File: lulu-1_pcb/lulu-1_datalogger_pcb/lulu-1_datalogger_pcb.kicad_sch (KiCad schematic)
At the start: 37 parts, among them J1 Conn_01x02_Pin, J2 SBH11-PBPC-D10-ST-BK, J3 MEM2067-02-180-00-A_REVB, SW1 SW_Nidec_CAS-120A1, U1 LP3982ILD-3.3, U2 STM32F401RETx, U3 BMP280, U4 MPU-6050, U5 W25Q16JVSS, Y1 25 Mhz, Y2 32 Khz

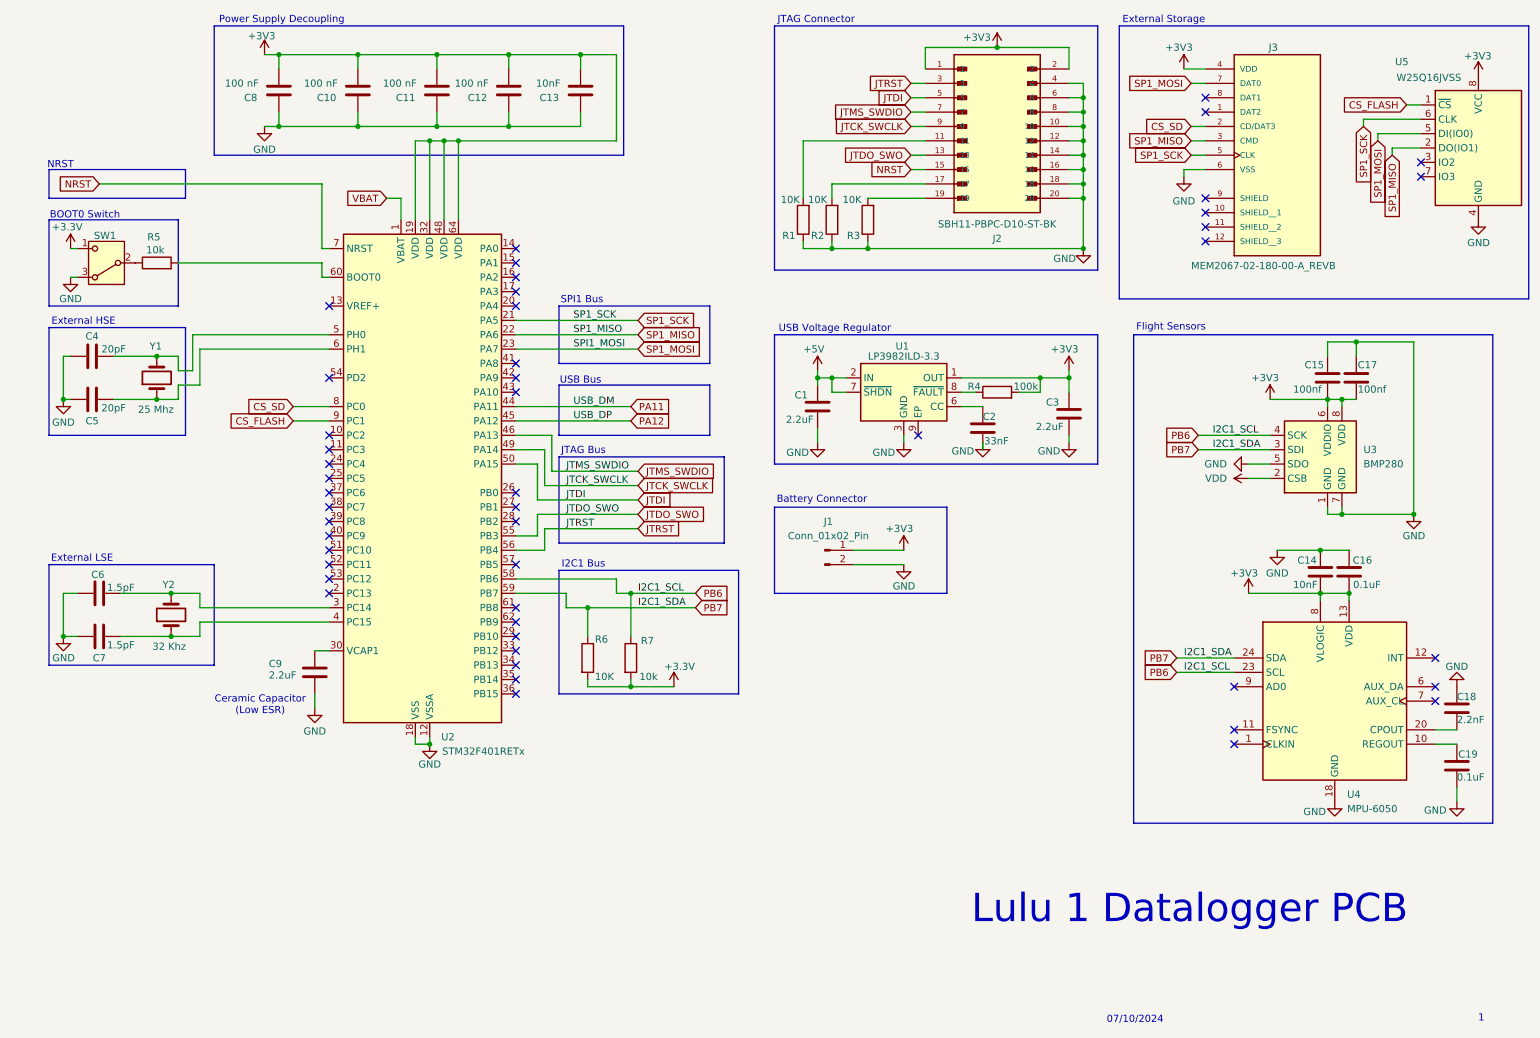
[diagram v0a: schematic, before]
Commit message: label for SPI chip select pins and remvoed VBAT and merged with +3V3/VDD pins
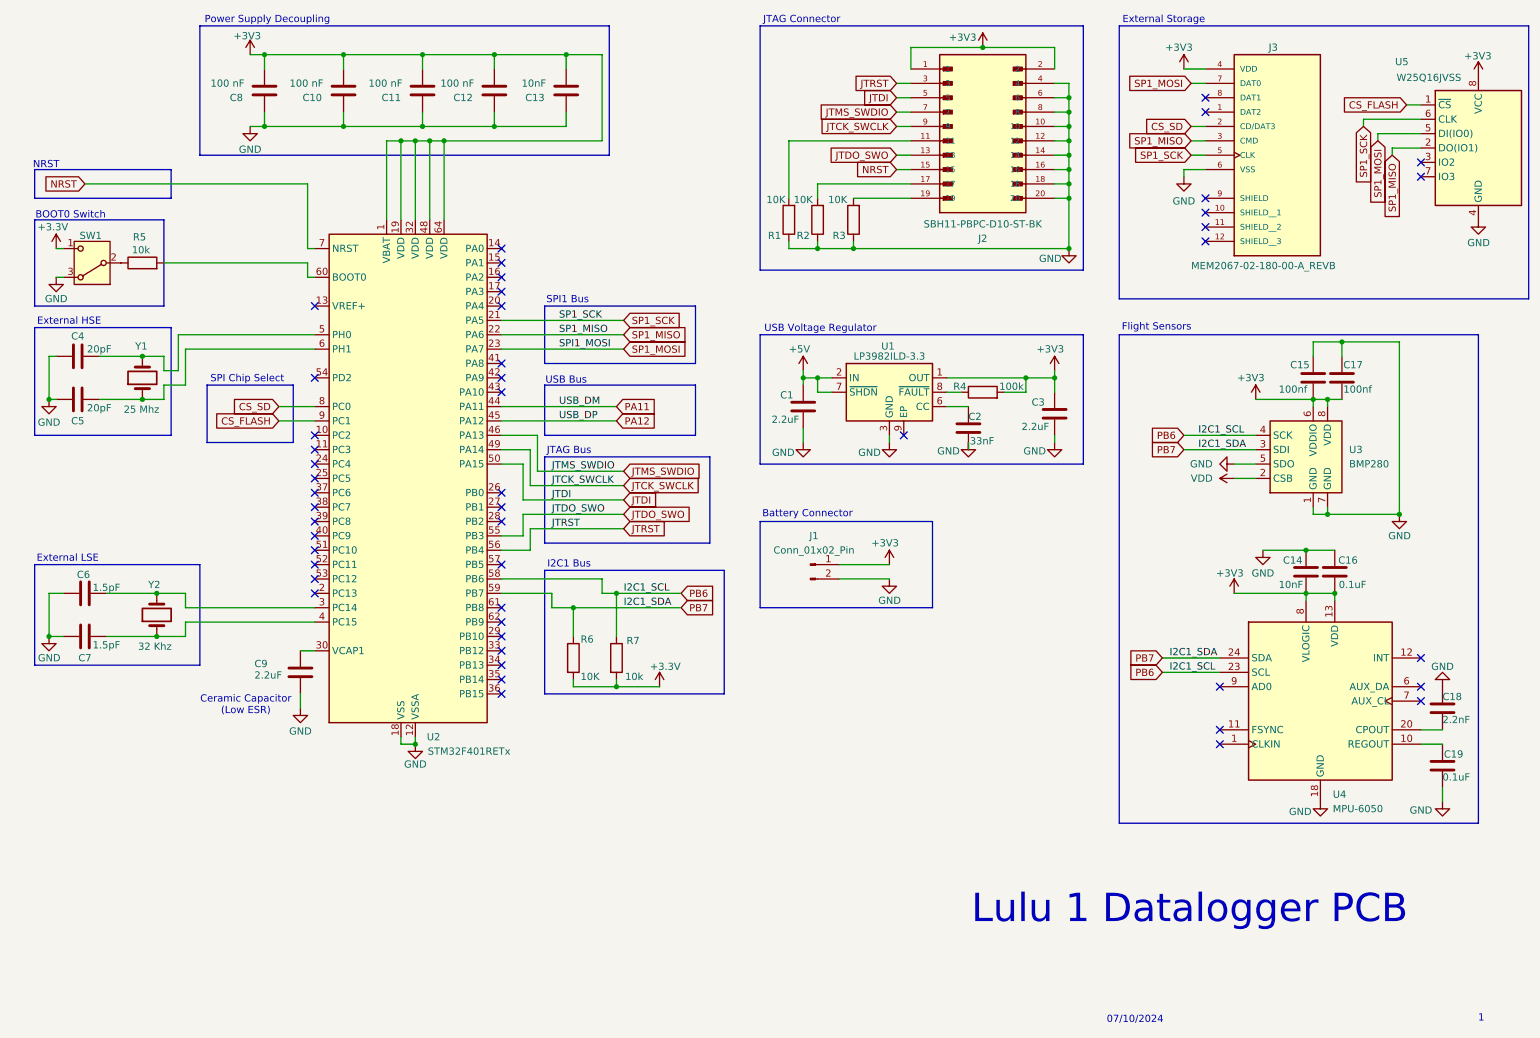
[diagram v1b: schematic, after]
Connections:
- net VBAT is gone; now on net +3V3: U2.1 (VBAT)
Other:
- note added: "SPI Chip Select"
- moved on the sheet: C1, C10, C11, C12, C13, C14, C15, C16, C17, C18, C19, C2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

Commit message: added reverse polarity protection diode
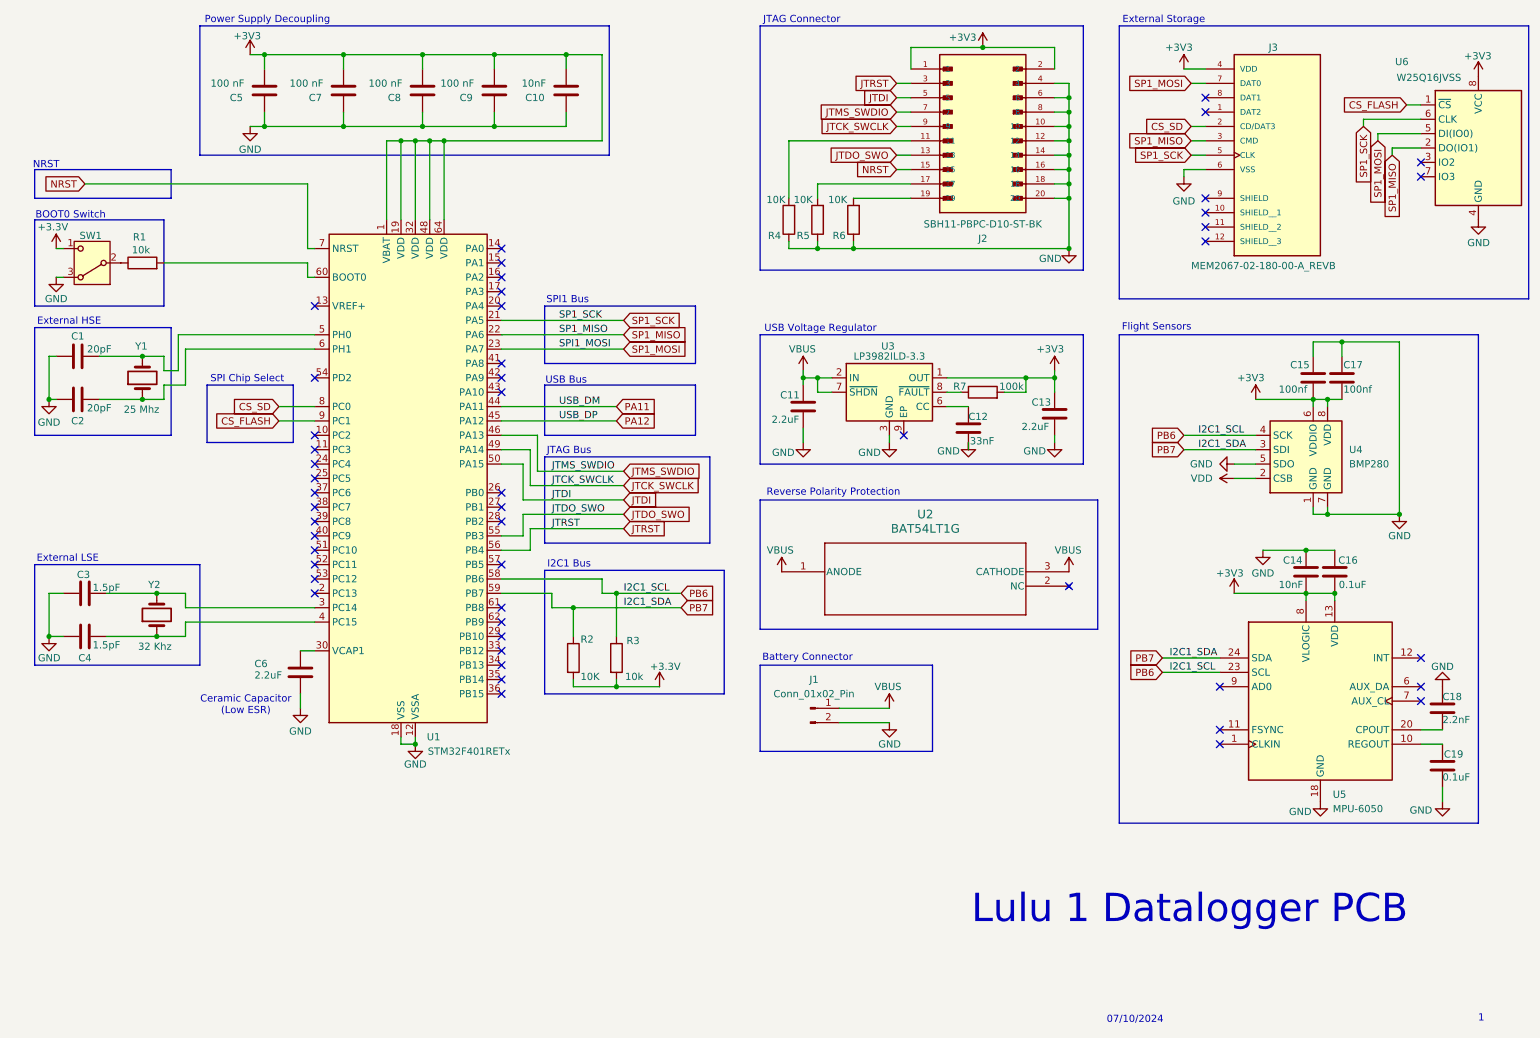
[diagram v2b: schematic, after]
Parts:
- added U2: BAT54LT1G, SOT-23-3_1P4X3P040_ONS, symbol 2024-10-18_23-00-30:BAT54LT1G
- renumbered C4 to C1, C13 to C10, C1 to C11, C2 to C12, C3 to C13, C5 to C2, C6 to C3, C7 to C4, C8 to C5, C9 to C6, C10 to C7, C11 to C8, C12 to C9, R5 to R1, R6 to R2, R7 to R3, R1 to R4, R2 to R5, R3 to R6, R4 to R7, U2 to U1, U1 to U3, U3 to U4, U4 to U5, U5 to U6
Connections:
- net +3V3: no longer J1.1 (Pin_1)
- net +5V renamed VBUS
- net VBUS: now also J1.1 (Pin_1), U2.1 (ANODE), U2.3 (CATHODE)
- no-connect marks 48 -> 49
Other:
- note added: "Reverse Polarity Protection"
- moved on the sheet: J1

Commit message: added JST-XH connector for 18650 LiIon battery
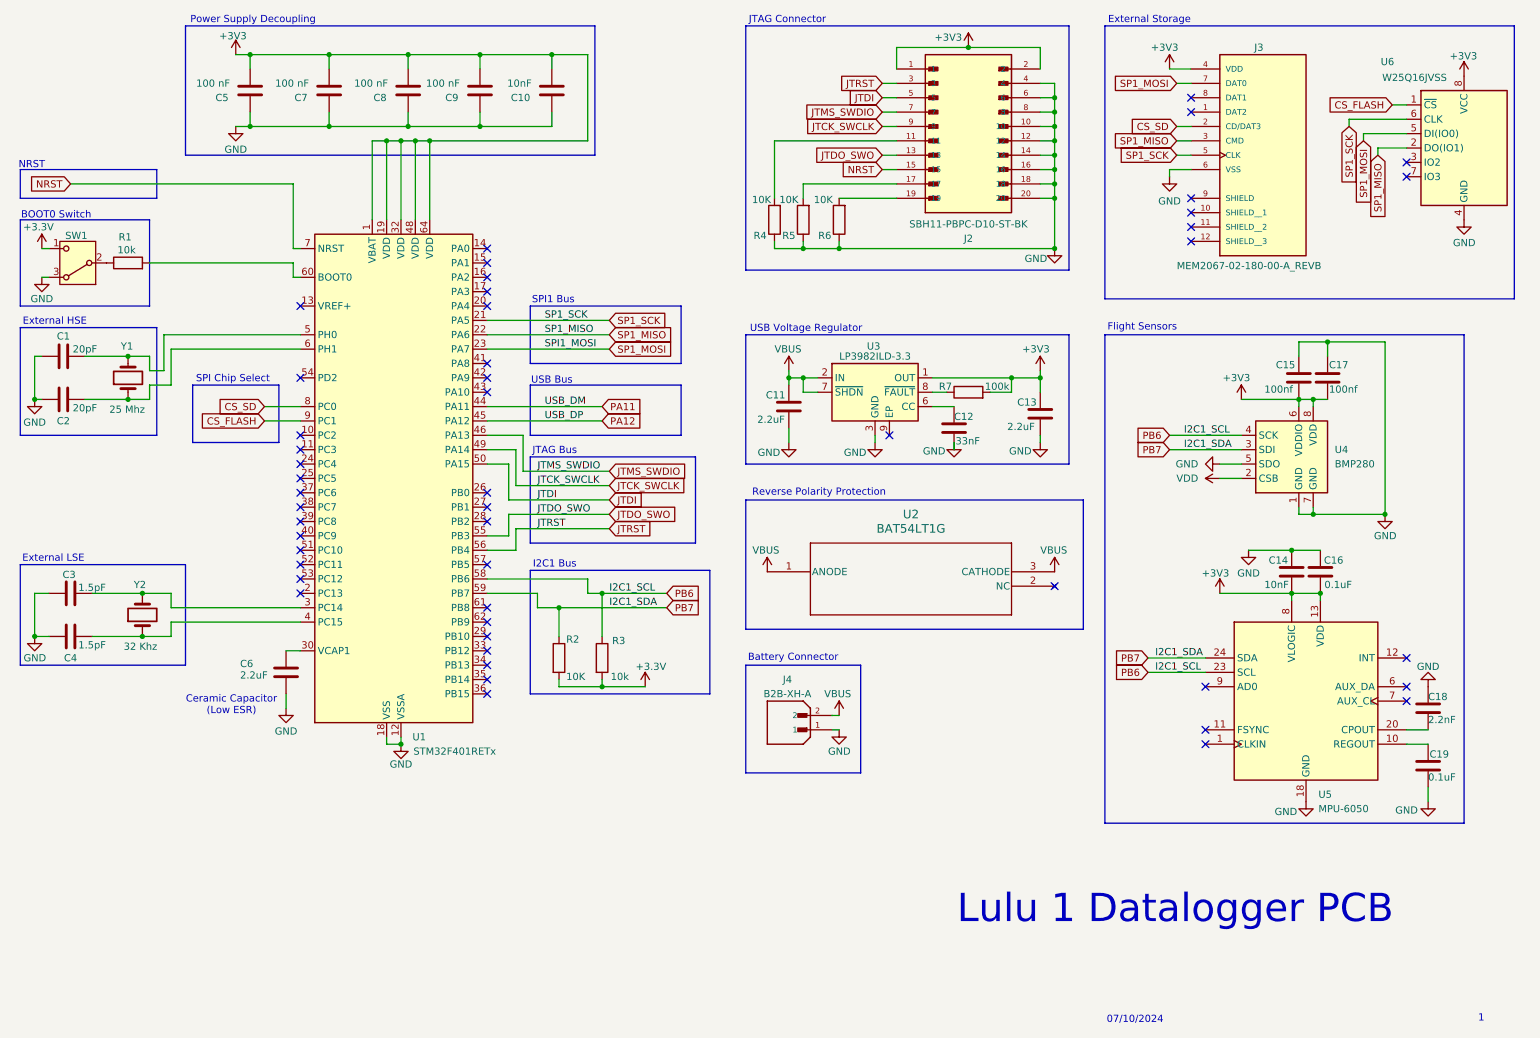
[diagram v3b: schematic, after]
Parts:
- removed J1: Conn_01x02_Pin, symbol Connector:Conn_01x02_Pin
- added J4: B2B-XH-A, B2B-XH-A:JST_B2B-XH-A, symbol B2B-XH-A:B2B-XH-A
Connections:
- net GND: now also J4.1
- net VBUS: now also J4.2
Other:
- moved on the sheet: C1, C10, C11, C12, C13, C14, C15, C16, C17, C18, C19, C2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

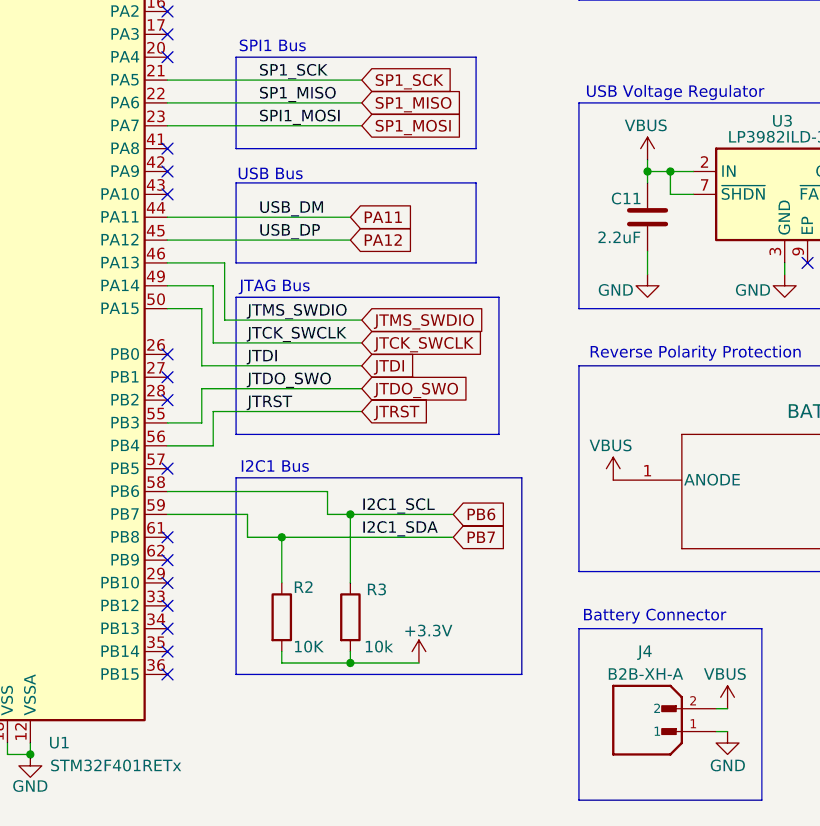
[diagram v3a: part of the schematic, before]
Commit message: removed usb bus pins from mcu
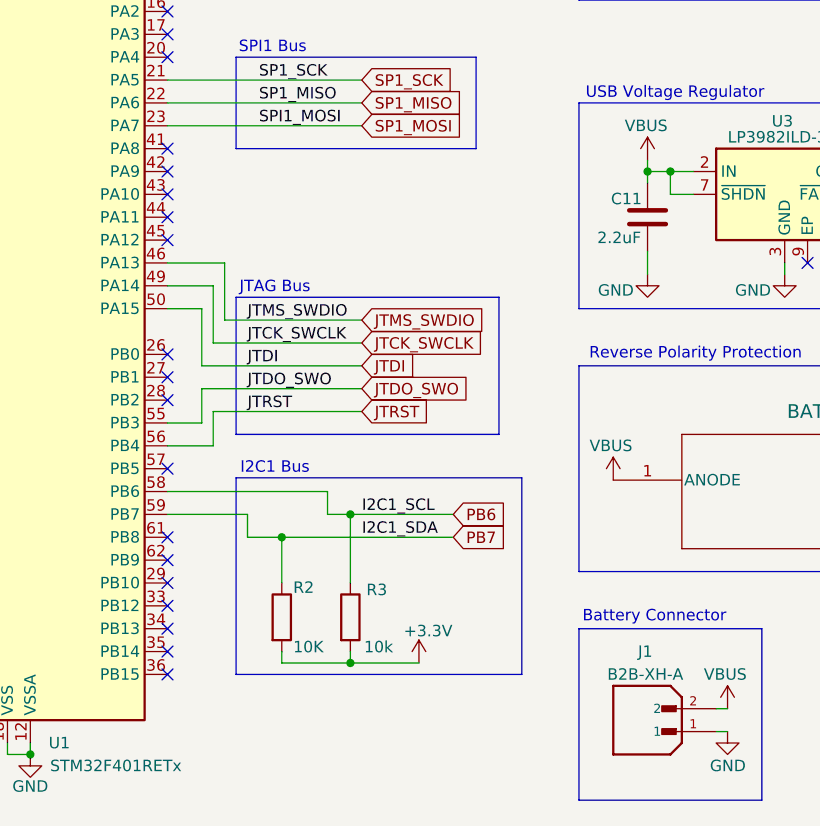
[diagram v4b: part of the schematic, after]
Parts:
- J1: renamed from J4; footprint B2B-XH-A:JST_B2B-XH-A -> B2B_XH_A:JST_B2B-XH-A
- J2: footprint SBH11-PBPC-D10-ST-BK:SULLINS_SBH11-PBPC-D10-ST-BK -> SBH11_PBPC_D10_ST_BK:SULLINS_SBH11-PBPC-D10-ST-BK
- J3: footprint MEM2067-02-180-00-A_REVB:GCT_MEM2067-02-180-00-A_REVB -> MEM2067_02_180_00_A:GCT_MEM2067-02-180-00-A_REVB
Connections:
- net PA11: no longer names the net of U1.44 (PA11)
- net PA12: no longer names the net of U1.45 (PA12)
- no-connect marks 49 -> 51
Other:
- note removed: "USB Bus"
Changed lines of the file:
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@@
 	)
 	(no_connect
+		(at 99.06 87.63)
+	)
+	(no_connect
 		(at 199.39 116.84)
 	)
@@
 	)
 	(no_connect
+		(at 99.06 85.09)
+	)
+	(no_connect
 		(at 99.06 128.27)
 	)
@@
 	(wire
 		(pts
-			(xy 99.06 85.09) (xy 119.38 85.09)
-		)
-		(stroke
-			(width 0)
-			(type default)
-		)
-	)
-	(wire
-		(pts
 			(xy 247.65 73.66) (xy 247.65 76.2)
 		)
@@
 	(wire
 		(pts
-			(xy 99.06 87.63) (xy 119.38 87.63)
-		)
-		(stroke
-			(width 0)
-			(type default)
-		)
-	)
-	(wire
-		(pts
 			(xy 241.3 110.49) (xy 246.38 110.49)
 		)
@@
 	)
 	(rectangle
-		(start 106.68 81.28)
-		(end 133.35 90.17)
-		(stroke
-			(width 0)
-			(type default)
-		)
-		(fill
-			(type none)
-		)
-	)
-	(rectangle
 		(start 208.28 17.78)
 		(end 280.67 66.04)
@@
 		)
 	)
-	(text "USB Bus\n"
-		(exclude_from_sim no)
-		(at 110.49 80.518 0)
-		(effects
-			(font
-				(size 1.27 1.27)
-			)
-		)
-	)
 	(text "NRST\n"
 		(exclude_from_sim no)
@@
 		)
 	)
-	(label "USB_DM"
-		(at 109.22 85.09 0)
-		(fields_autoplaced yes)
-		(effects
-			(font
-				(size 1.27 1.27)
-			)
-			(justify left bottom)
-		)
-	)
 	(label "JTMS_SWDIO"
 		(at 107.95 96.52 0)
@@
 		)
 	)
-	(label "USB_DP"
-		(at 109.22 87.63 0)
-		(fields_autoplaced yes)
-		(effects
-			(font
-				(size 1.27 1.27)
-			)
-			(justify left bottom)
-		)
-	)
 	(label "SP1_SCK"
 		(at 109.22 69.85 0)
@@
 		)
 	)
-	(global_label "PA11"
-		(shape input)
-		(at 119.38 85.09 0)
-		(fields_autoplaced yes)
-		(effects
-			(font
-				(size 1.27 1.27)
-			)
-			(justify left)
-		)
-		(property "Intersheetrefs" "${INTERSHEET_REFS}"
-			(at 127.1428 85.09 0)
-			(effects
-				(font
-					(size 1.27 1.27)
-				)
-				(justify left)
-				(hide yes)
-			)
-		)
-	)
 	(global_label "SP1_MOSI"
 		(shape input)
@@
 		)
 	)
-	(global_label "PA12"
-		(shape input)
-		(at 119.38 87.63 0)
-		(fields_autoplaced yes)
-		(effects
-			(font
-				(size 1.27 1.27)
-			)
-			(justify left)
-		)
-		(property "Intersheetrefs" "${INTERSHEET_REFS}"
-			(at 127.1428 87.63 0)
-			(effects
-				(font
-					(size 1.27 1.27)
-				)
-				(justify left)
-				(hide yes)
-			)
-		)
-	)
 	(global_label "JTDO_SWO"
 		(shape input)
@@
 			)
 		)
-		(property "Footprint" "SBH11-PBPC-D10-ST-BK:SULLINS_SBH11-PBPC-D10-ST-BK"
+		(property "Footprint" "SBH11_PBPC_D10_ST_BK:SULLINS_SBH11-PBPC-D10-ST-BK"
 			(at 184.15 38.1 0)
 			(effects
@@
 			)
 		)
-		(property "Footprint" "MEM2067-02-180-00-A_REVB:GCT_MEM2067-02-180-00-A_REVB"
+		(property "Footprint" "MEM2067_02_180_00_A:GCT_MEM2067-02-180-00-A_REVB"
 			(at 228.6 35.56 0)
 			(effects
@@
 		(on_board yes)
 		(dnp no)
-		(property "Reference" "J4"
+		(property "Reference" "J1"
 			(at 152.146 133.35 0)
 			(effects
@@
 			)
 		)
-		(property "Footprint" "B2B-XH-A:JST_B2B-XH-A"
+		(property "Footprint" "B2B_XH_A:JST_B2B-XH-A"
 			(at 152.4 139.7 0)
 			(effects
@@
 			(project ""
 				(path "/34f83adb-7c37-4d95-be2d-ff70244d0c69"
-					(reference "J4")
+					(reference "J1")
 					(unit 1)
 				)
@@
 		(on_board yes)
 		(dnp no)
-		(property "Reference" "#PWR036"
+		(property "Reference" "#PWR013"
 			(at 161.29 143.51 0)
 			(effects
@@
 			(project "lulu-1_datalogger_pcb"
 				(path "/34f83adb-7c37-4d95-be2d-ff70244d0c69"
-					(reference "#PWR036")
+					(reference "#PWR013")
 					(unit 1)
 				)
@@
 		(on_board yes)
 		(dnp no)
-		(property "Reference" "#PWR035"
+		(property "Reference" "#PWR014"
 			(at 161.29 148.59 0)
 			(effects
@@
 			(project "lulu-1_datalogger_pcb"
 				(path "/34f83adb-7c37-4d95-be2d-ff70244d0c69"
-					(reference "#PWR035")
+					(reference "#PWR014")
 					(unit 1)
 				)
@@
 		(on_board yes)
 		(dnp no)
-		(property "Reference" "#PWR013"
+		(property "Reference" "#PWR015"
 			(at 167.64 97.79 0)
 			(effects
@@
 			(project "lulu-1_datalogger_pcb"
 				(path "/34f83adb-7c37-4d95-be2d-ff70244d0c69"
-					(reference "#PWR013")
+					(reference "#PWR015")
 					(unit 1)
 				)
